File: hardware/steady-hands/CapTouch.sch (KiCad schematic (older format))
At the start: 5 parts

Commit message: Adds power management components
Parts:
- C?: symbol steady-hands:CapSense_01x08 -> Sij_Touch:CapSense_01x08
- U?: symbol steady-hands:CPT112S-A02-GM -> Sij_Touch:CPT112S-A02-GM
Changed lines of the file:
@@
 $EndComp
 $Comp
-L steady-hands:CapSense_01x08 C?
+L Sij_Touch:CapSense_01x08 C?
 U 1 1 5EFBC936
 P 7550 4450
@@
 Connection ~ 3350 4200
 $Comp
-L steady-hands:CPT112S-A02-GM U?
+L Sij_Touch:CPT112S-A02-GM U?
 U 1 1 5EF85C6E
 P 6050 5500

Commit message: Edits power management components
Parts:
- U?: symbol Sij_Touch:CPT112S-A02-GM -> steady-hands:CPT112S-A02-GM
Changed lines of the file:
@@
 Connection ~ 3350 4200
 $Comp
-L Sij_Touch:CPT112S-A02-GM U?
+L steady-hands:CPT112S-A02-GM U?
 U 1 1 5EF85C6E
 P 6050 5500

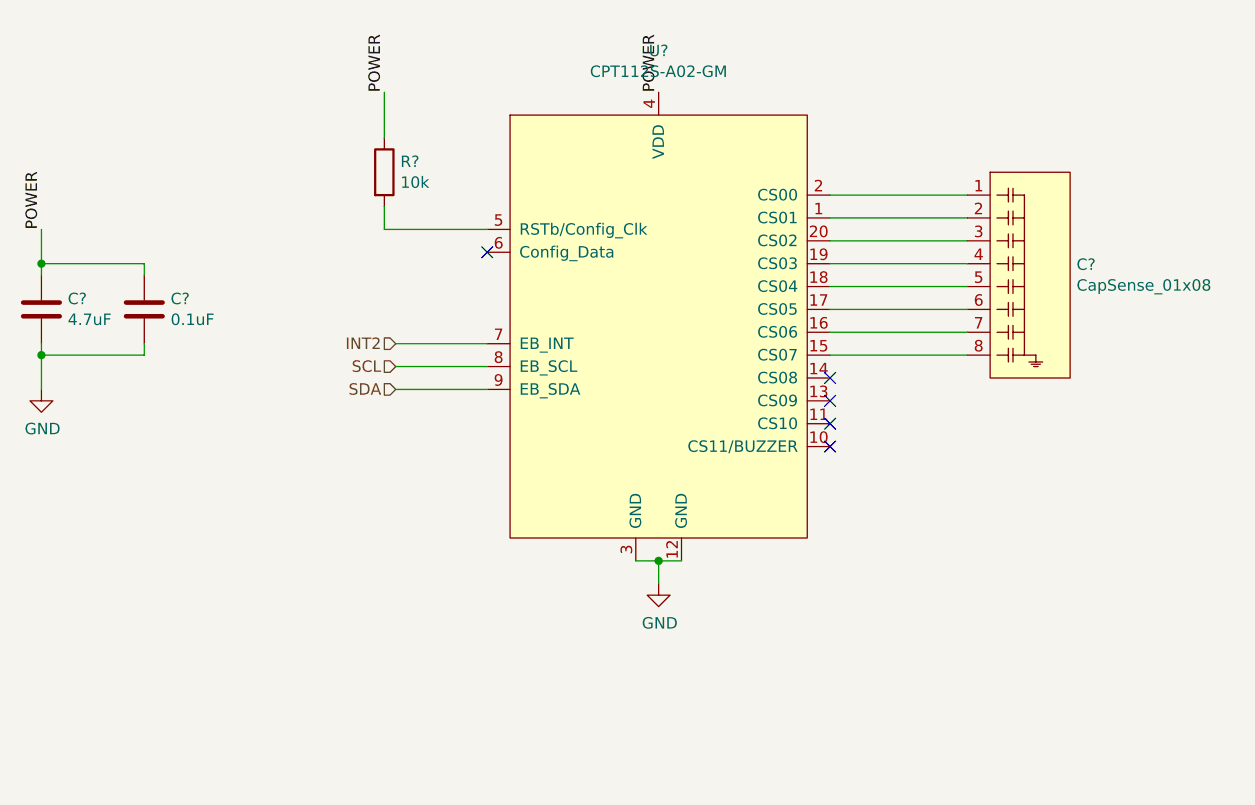
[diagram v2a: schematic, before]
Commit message: Completes schematic connections
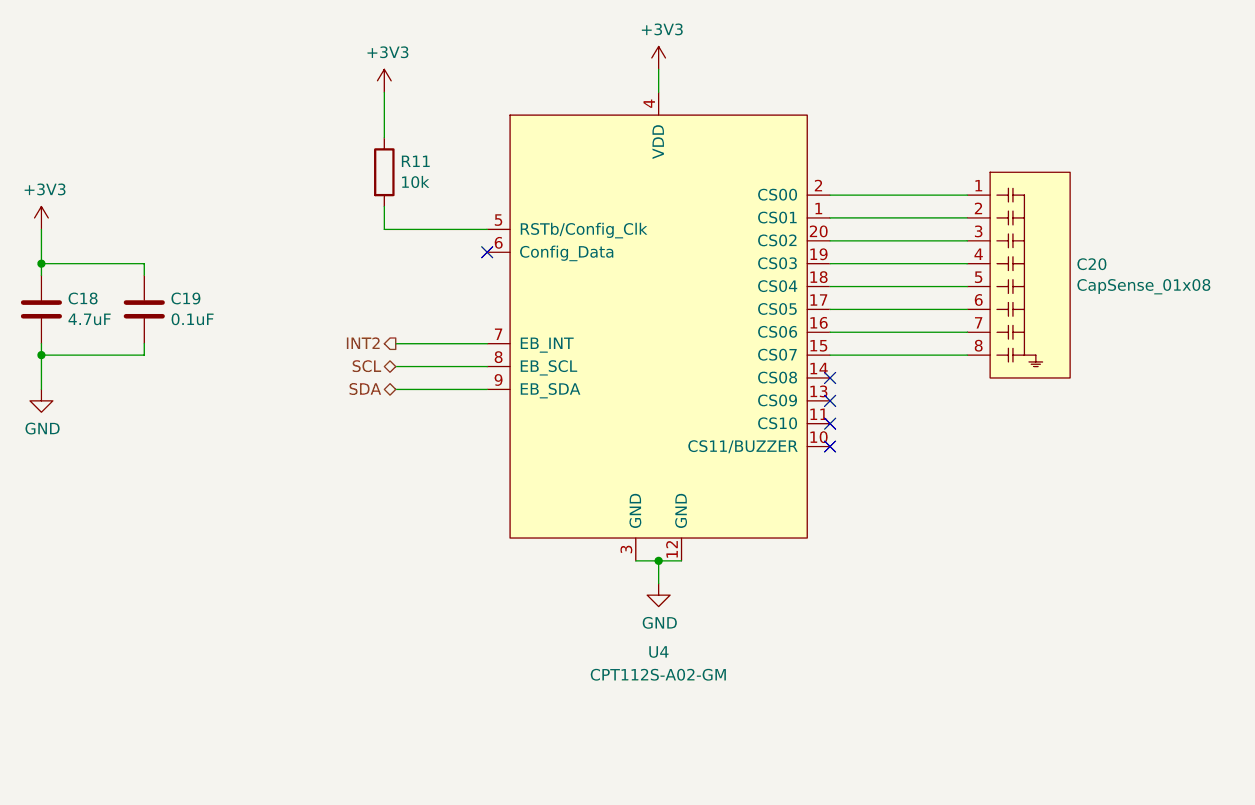
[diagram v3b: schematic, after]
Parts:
- gave numbers to parts that had none: 5
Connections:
- net POWER renamed +3V3
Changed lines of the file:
@@
 Wire Wire Line
 	5300 4350 4900 4350
-Text HLabel 4900 4150 0    50   Input ~ 0
+Text HLabel 4900 4150 0    50   Output ~ 0
 INT2
-Text HLabel 4900 4250 0    50   Input ~ 0
+Text HLabel 4900 4250 0    50   BiDi ~ 0
 SCL
-Text HLabel 4900 4350 0    50   Input ~ 0
+Text HLabel 4900 4350 0    50   BiDi ~ 0
 SDA
 $Comp
-L Device:C C?
+L Device:C C18
 U 1 1 5EF414DE
 P 3350 4000
-F 0 "C?" H 3465 4046 50  0000 L CNN
+F 0 "C18" H 3465 4046 50  0000 L CNN
 F 1 "4.7uF" H 3465 3955 50  0000 L CNN
 F 2 "" H 3388 3850 50  0001 C CNN
@@
 $EndComp
 $Comp
-L Device:C C?
+L Device:C C19
 U 1 1 5EF4247D
 P 3800 4000
-F 0 "C?" H 3915 4046 50  0000 L CNN
+F 0 "C19" H 3915 4046 50  0000 L CNN
 F 1 "0.1uF" H 3915 3955 50  0000 L CNN
 F 2 "" H 3838 3850 50  0001 C CNN
@@
 $EndComp
 $Comp
-L Sij_Touch:CapSense_01x08 C?
+L Sij_Touch:CapSense_01x08 C20
 U 1 1 5EFBC936
 P 7550 4450
-F 0 "C?" H 7878 5096 50  0000 L CNN
+F 0 "C20" H 7878 5096 50  0000 L CNN
 F 1 "CapSense_01x08" H 7878 5005 50  0000 L CNN
 F 2 "Sij_Touch:TouchSlider-8_35x10mm" H 7550 4450 50  0001 C CNN
@@
 $EndComp
 $Comp
-L power:GND #PWR?
+L power:GND #PWR0132
 U 1 1 5EF589C1
 P 6050 5200
-F 0 "#PWR?" H 6050 4950 50  0001 C CNN
+F 0 "#PWR0132" H 6050 4950 50  0001 C CNN
 F 1 "GND" H 6055 5027 50  0000 C CNN
 F 2 "" H 6050 5200 50  0001 C CNN
@@
 Wire Wire Line
 	3350 3800 3350 3650
-Text Label 3350 3650 1    50   ~ 0
-POWER
 Wire Wire Line
 	3350 4200 3350 4350
 $Comp
-L power:GND #PWR?
+L power:GND #PWR0133
 U 1 1 5EF5D4FE
 P 3350 4350
-F 0 "#PWR?" H 3350 4100 50  0001 C CNN
+F 0 "#PWR0133" H 3350 4100 50  0001 C CNN
 F 1 "GND" H 3355 4177 50  0000 C CNN
 F 2 "" H 3350 4350 50  0001 C CNN
@@
 Connection ~ 3350 4200
 $Comp
-L steady-hands:CPT112S-A02-GM U?
+L steady-hands:CPT112S-A02-GM U4
 U 1 1 5EF85C6E
 P 6050 5500
-F 0 "U?" H 6050 8131 50  0000 C CNN
-F 1 "CPT112S-A02-GM" H 6050 8040 50  0000 C CNN
+F 0 "U4" H 6050 5500 50  0000 C CNN
+F 1 "CPT112S-A02-GM" H 6050 5400 50  0000 C CNN
 F 2 "" H 6050 5500 50  0001 C CNN
 F 3 "https://www.mouser.com/datasheet/2/368/CPT112S-DataSheet-1397794.pdf" H 6050 5500 50  0001 C CNN
@@
 	6050 5100 6150 5100
 $Comp
-L Device:R R?
+L Device:R R11
 U 1 1 5EF98D5D
 P 4850 3400
-F 0 "R?" H 4920 3446 50  0000 L CNN
+F 0 "R11" H 4920 3446 50  0000 L CNN
 F 1 "10k" H 4920 3355 50  0000 L CNN
 F 2 "" V 4780 3400 50  0001 C CNN
@@
 Wire Wire Line
 	4850 3250 4850 3050
-Text Label 4850 3050 1    50   ~ 0
-POWER
-Text Label 6050 3050 1    50   ~ 0
-POWER
+Wire Wire Line
+	6050 3050 6050 2950
+$Comp
+L power:+3V3 #PWR0134
+U 1 1 5F161753
+P 6050 2950
+F 0 "#PWR0134" H 6050 2800 50  0001 C CNN
+F 1 "+3V3" H 6065 3123 50  0000 C CNN
+F 2 "" H 6050 2950 50  0001 C CNN
+F 3 "" H 6050 2950 50  0001 C CNN
+	1    6050 2950
+	1    0    0    -1
+$EndComp
+$Comp
+L power:+3V3 #PWR0135
+U 1 1 5F1618F5
+P 4850 3050
+F 0 "#PWR0135" H 4850 2900 50  0001 C CNN
+F 1 "+3V3" H 4865 3223 50  0000 C CNN
+F 2 "" H 4850 3050 50  0001 C CNN
+F 3 "" H 4850 3050 50  0001 C CNN
+	1    4850 3050
+	1    0    0    -1
+$EndComp
+$Comp
+L power:+3V3 #PWR0136
+U 1 1 5F161AA4
+P 3350 3650
+F 0 "#PWR0136" H 3350 3500 50  0001 C CNN
+F 1 "+3V3" H 3365 3823 50  0000 C CNN
+F 2 "" H 3350 3650 50  0001 C CNN
+F 3 "" H 3350 3650 50  0001 C CNN
+	1    3350 3650
+	1    0    0    -1
+$EndComp
 $EndSCHEMATC
